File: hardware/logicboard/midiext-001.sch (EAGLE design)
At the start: 25 parts, among them IC1 74ALS05N, IC2 LTC485N, IC3 LTC485N, J1 MIDIIN, J2 MIDIOUT, J3 PWR, J4 LED, J5 MIDITX, J6 MIDIRX

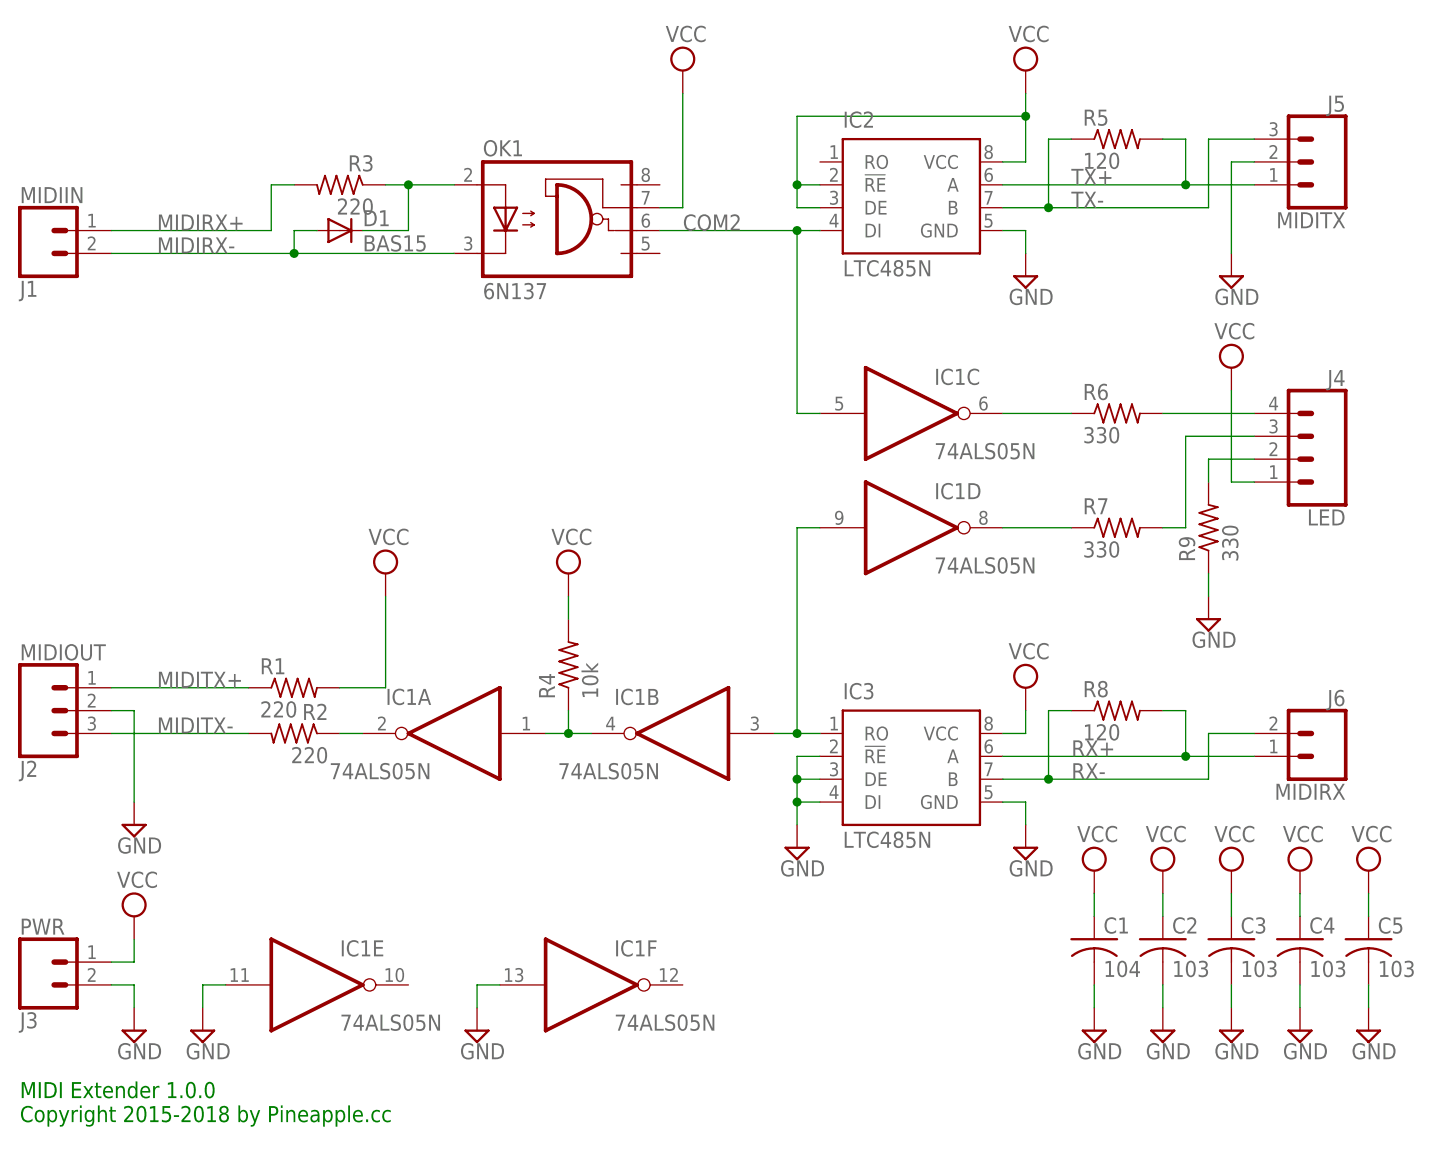
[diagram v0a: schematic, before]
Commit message: Changed layout.
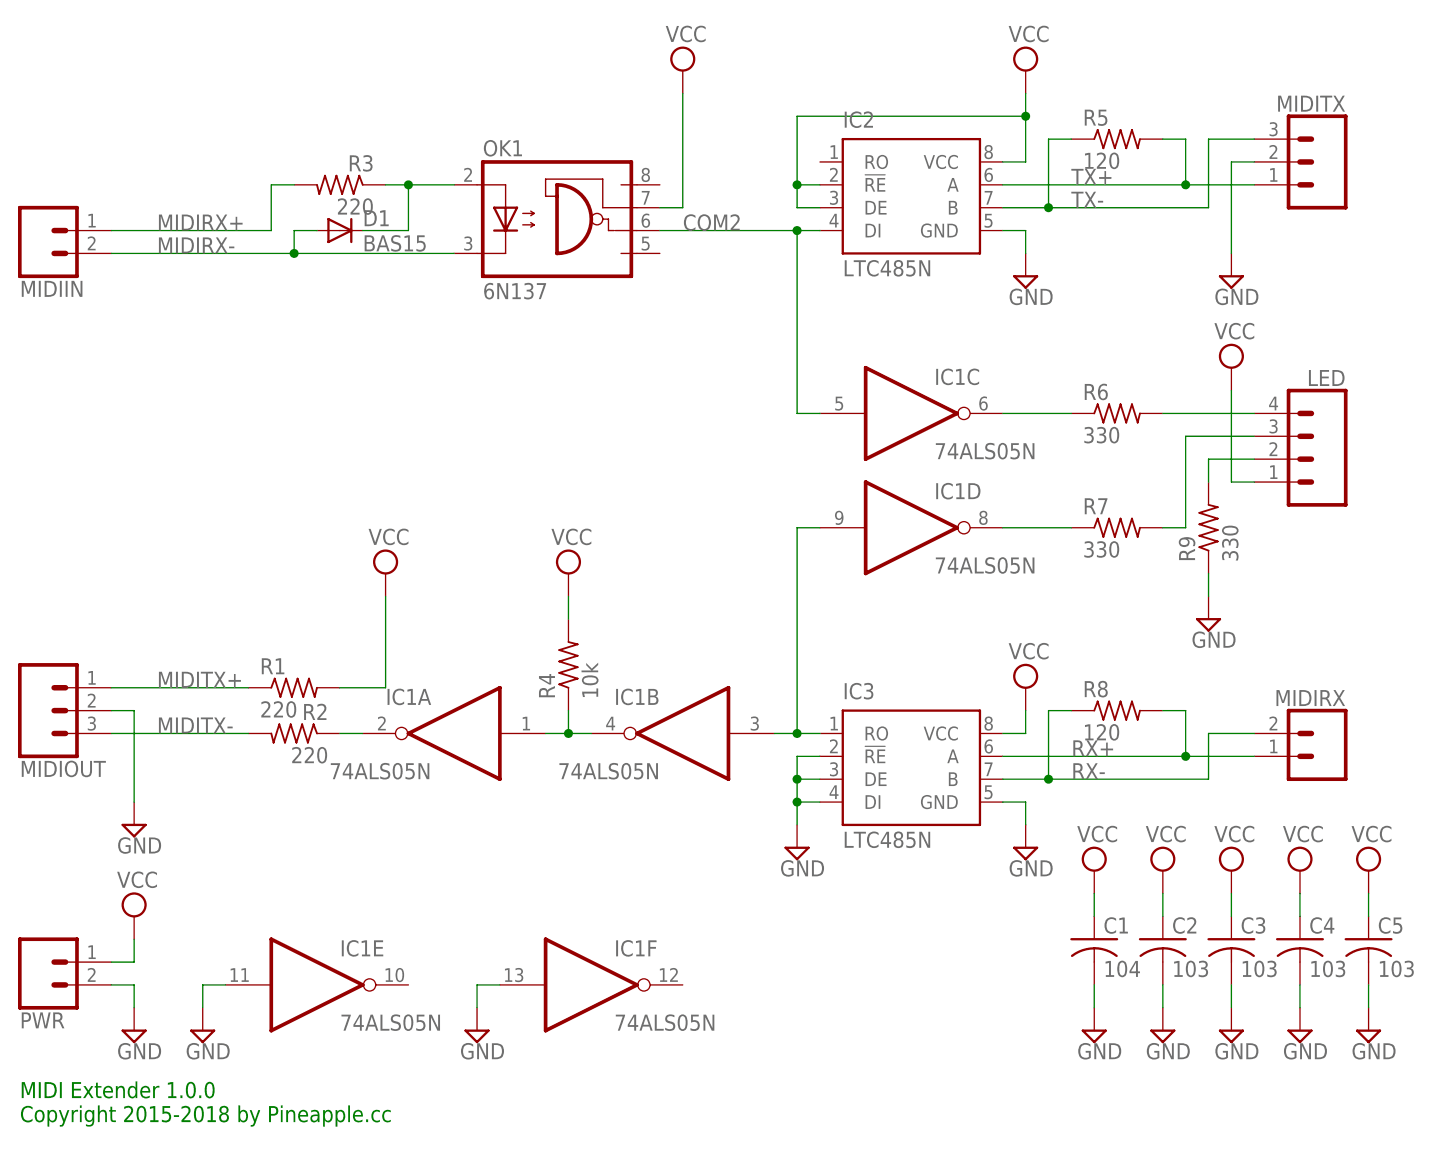
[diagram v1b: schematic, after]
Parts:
- LED: value LED -> (none)
- MIDIIN: value MIDIIN -> (none)
- MIDIOUT: value MIDIOUT -> (none)
- MIDIRX: value MIDIRX -> (none)
- MIDITX: value MIDITX -> (none)
- PWR: value PWR -> (none)
- renumbered J1 to MIDIIN, J2 to MIDIOUT, J3 to PWR, J4 to LED, J5 to MIDITX, J6 to MIDIRX
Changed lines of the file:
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@@
 <setting verticaltext="up"/>
 </settings>
-<grid distance="0.1" unitdist="inch" unit="inch" style="lines" multiple="1" display="no" altdistance="0.01" altunitdist="inch" altunit="inch"/>
+<grid distance="0.1" unitdist="inch" unit="inch" style="lines" multiple="1" display="yes" altdistance="0.01" altunitdist="inch" altunit="inch"/>
 <layers>
 <layer number="1" name="Top" color="4" fill="1" visible="no" active="no"/>
@@
 <part name="SUPPLY1" library="supply2" library_urn="urn:adsk.eagle:library:372" deviceset="GND" device=""/>
 <part name="SUPPLY19" library="supply2" library_urn="urn:adsk.eagle:library:372" deviceset="GND" device=""/>
-<part name="J3" library="SparkFun-Connectors" deviceset="CONN_02" device="JST-PTH-2" value="PWR"/>
-<part name="J1" library="SparkFun-Connectors" deviceset="CONN_02" device="JST-PTH-2" value="MIDIIN"/>
-<part name="J6" library="SparkFun-Connectors" deviceset="CONN_02" device="JST-PTH-2" value="MIDIRX"/>
-<part name="J2" library="SparkFun-Connectors" deviceset="CONN_03" device="JST-PTH" value="MIDIOUT"/>
-<part name="J5" library="SparkFun-Connectors" deviceset="CONN_03" device="JST-PTH" value="MIDITX"/>
-<part name="J4" library="SparkFun-Connectors" deviceset="CONN_04" device="JST-PTH" value="LED"/>
+<part name="PWR" library="SparkFun-Connectors" deviceset="CONN_02" device="JST-PTH-2"/>
+<part name="MIDIIN" library="SparkFun-Connectors" deviceset="CONN_02" device="JST-PTH-2"/>
+<part name="MIDIRX" library="SparkFun-Connectors" deviceset="CONN_02" device="JST-PTH-2"/>
+<part name="MIDIOUT" library="SparkFun-Connectors" deviceset="CONN_03" device="JST-PTH"/>
+<part name="MIDITX" library="SparkFun-Connectors" deviceset="CONN_03" device="JST-PTH"/>
+<part name="LED" library="SparkFun-Connectors" deviceset="CONN_04" device="JST-PTH"/>
 <part name="IC1" library="74xx-eu" library_urn="urn:adsk.eagle:library:85" deviceset="74*05" device="N" package3d_urn="urn:adsk.eagle:package:2008/1" technology="ALS"/>
 <part name="R4" library="resistor" library_urn="urn:adsk.eagle:library:348" deviceset="R-US_" device="0204/5" package3d_urn="urn:adsk.eagle:package:25955/1" value="10k"/>
@@
 <instance part="SUPPLY1" gate="GND" x="15.24" y="35.56"/>
 <instance part="SUPPLY19" gate="GND" x="137.16" y="96.52"/>
-<instance part="J3" gate="G$1" x="5.08" y="20.32" rot="MR180"/>
-<instance part="J1" gate="G$1" x="5.08" y="101.6" rot="MR180"/>
-<instance part="J6" gate="G$1" x="147.32" y="43.18" rot="MR0"/>
-<instance part="J2" gate="J$1" x="5.08" y="48.26" rot="MR180"/>
-<instance part="J5" gate="J$1" x="147.32" y="109.22" rot="MR0"/>
-<instance part="J4" gate="G$1" x="144.78" y="76.2" rot="MR0"/>
+<instance part="PWR" gate="G$1" x="5.08" y="20.32" rot="MR180"/>
+<instance part="MIDIIN" gate="G$1" x="5.08" y="101.6" rot="MR180"/>
+<instance part="MIDIRX" gate="G$1" x="147.32" y="43.18" rot="MR0"/>
+<instance part="MIDIOUT" gate="J$1" x="5.08" y="48.26" rot="MR180"/>
+<instance part="MIDITX" gate="J$1" x="147.32" y="109.22" rot="MR0"/>
+<instance part="LED" gate="G$1" x="144.78" y="76.2" rot="MR0"/>
 <instance part="IC1" gate="A" x="50.8" y="45.72" rot="MR0"/>
 <instance part="IC1" gate="B" x="76.2" y="45.72" rot="MR0"/>
@@
 <pinref part="SUPPLY3" gate="GND" pin="GND"/>
 <wire x1="15.24" y1="17.78" x2="15.24" y2="15.24" width="0.1524" layer="91"/>
-<pinref part="J3" gate="G$1" pin="2"/>
+<pinref part="PWR" gate="G$1" pin="2"/>
 </segment>
 <segment>
@@
 <wire x1="12.7" y1="48.26" x2="15.24" y2="48.26" width="0.1524" layer="91"/>
 <wire x1="15.24" y1="48.26" x2="15.24" y2="38.1" width="0.1524" layer="91"/>
-<pinref part="J2" gate="J$1" pin="2"/>
+<pinref part="MIDIOUT" gate="J$1" pin="2"/>
 </segment>
 <segment>
@@
 <pinref part="SUPPLY19" gate="GND" pin="GND"/>
 <wire x1="137.16" y1="109.22" x2="137.16" y2="99.06" width="0.1524" layer="91"/>
-<pinref part="J5" gate="J$1" pin="2"/>
+<pinref part="MIDITX" gate="J$1" pin="2"/>
 </segment>
 <segment>
@@
 <wire x1="15.24" y1="22.86" x2="15.24" y2="20.32" width="0.1524" layer="91"/>
 <wire x1="15.24" y1="20.32" x2="12.7" y2="20.32" width="0.1524" layer="91"/>
-<pinref part="J3" gate="G$1" pin="1"/>
+<pinref part="PWR" gate="G$1" pin="1"/>
 </segment>
 <segment>
@@
 <pinref part="SUPPLY20" gate="G$1" pin="VCC"/>
 <wire x1="137.16" y1="83.82" x2="137.16" y2="73.66" width="0.1524" layer="91"/>
-<pinref part="J4" gate="G$1" pin="1"/>
+<pinref part="LED" gate="G$1" pin="1"/>
 <wire x1="137.16" y1="73.66" x2="139.7" y2="73.66" width="0.1524" layer="91"/>
 </segment>
@@
 <wire x1="139.7" y1="106.68" x2="132.08" y2="106.68" width="0.1524" layer="91"/>
 <junction x="132.08" y="106.68"/>
-<pinref part="J5" gate="J$1" pin="1"/>
+<pinref part="MIDITX" gate="J$1" pin="1"/>
 </segment>
 </net>
@@
 <wire x1="50.8" y1="99.06" x2="33.02" y2="99.06" width="0.1524" layer="91"/>
 <junction x="33.02" y="99.06"/>
-<pinref part="J1" gate="G$1" pin="2"/>
+<pinref part="MIDIIN" gate="G$1" pin="2"/>
 </segment>
 </net>
@@
 <wire x1="132.08" y1="43.18" x2="139.7" y2="43.18" width="0.1524" layer="91"/>
 <junction x="132.08" y="43.18"/>
-<pinref part="J6" gate="G$1" pin="1"/>
+<pinref part="MIDIRX" gate="G$1" pin="1"/>
 </segment>
 </net>
@@
 <wire x1="134.62" y1="40.64" x2="116.84" y2="40.64" width="0.1524" layer="91"/>
 <junction x="116.84" y="40.64"/>
-<pinref part="J6" gate="G$1" pin="2"/>
+<pinref part="MIDIRX" gate="G$1" pin="2"/>
 </segment>
 </net>
@@
 <wire x1="139.7" y1="111.76" x2="134.62" y2="111.76" width="0.1524" layer="91"/>
 <wire x1="134.62" y1="111.76" x2="134.62" y2="104.14" width="0.1524" layer="91"/>
-<pinref part="J5" gate="J$1" pin="3"/>
+<pinref part="MIDITX" gate="J$1" pin="3"/>
 </segment>
 </net>
@@
 <wire x1="30.48" y1="106.68" x2="30.48" y2="101.6" width="0.1524" layer="91"/>
 <wire x1="30.48" y1="101.6" x2="12.7" y2="101.6" width="0.1524" layer="91"/>
-<pinref part="J1" gate="G$1" pin="1"/>
+<pinref part="MIDIIN" gate="G$1" pin="1"/>
 </segment>
 </net>
@@
 <wire x1="12.7" y1="45.72" x2="27.94" y2="45.72" width="0.1524" layer="91"/>
 <label x="17.78" y="45.72" size="1.778" layer="95"/>
-<pinref part="J2" gate="J$1" pin="3"/>
+<pinref part="MIDIOUT" gate="J$1" pin="3"/>
 </segment>
 </net>
@@
 <wire x1="12.7" y1="50.8" x2="27.94" y2="50.8" width="0.1524" layer="91"/>
 <label x="17.78" y="50.8" size="1.778" layer="95"/>
-<pinref part="J2" gate="J$1" pin="1"/>
+<pinref part="MIDIOUT" gate="J$1" pin="1"/>
 </segment>
 </net>
@@
 <net name="N$8" class="0">
 <segment>
-<pinref part="J4" gate="G$1" pin="4"/>
+<pinref part="LED" gate="G$1" pin="4"/>
 <pinref part="R6" gate="G$1" pin="2"/>
 <wire x1="139.7" y1="81.28" x2="129.54" y2="81.28" width="0.1524" layer="91"/>
@@
 <net name="N$9" class="0">
 <segment>
-<pinref part="J4" gate="G$1" pin="3"/>
+<pinref part="LED" gate="G$1" pin="3"/>
 <wire x1="139.7" y1="78.74" x2="132.08" y2="78.74" width="0.1524" layer="91"/>
 <wire x1="132.08" y1="78.74" x2="132.08" y2="68.58" width="0.1524" layer="91"/>
@@
 <net name="N$10" class="0">
 <segment>
-<pinref part="J4" gate="G$1" pin="2"/>
+<pinref part="LED" gate="G$1" pin="2"/>
 <wire x1="139.7" y1="76.2" x2="134.62" y2="76.2" width="0.1524" layer="91"/>
 <pinref part="R9" gate="G$1" pin="2"/>

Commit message: Changed silk pattern.
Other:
- note added: "MIDI Longranger 1.0.0 Copyright 2015-2018 by Pineapple.cc"
- note removed: "MIDI Extender 1.0.0 Copyright 2015-2018 by Pineapple.cc"
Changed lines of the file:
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@@
 <sheet>
 <plain>
-<text x="2.54" y="2.54" size="1.778" layer="91">MIDI Extender 1.0.0
+<text x="2.54" y="2.54" size="1.778" layer="91">MIDI Longranger 1.0.0
 Copyright 2015-2018 by Pineapple.cc</text>
 </plain>
